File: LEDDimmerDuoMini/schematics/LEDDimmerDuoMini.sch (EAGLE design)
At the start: 17 parts, among them IC1 7805T, T1 2N3904, T2 2N3904

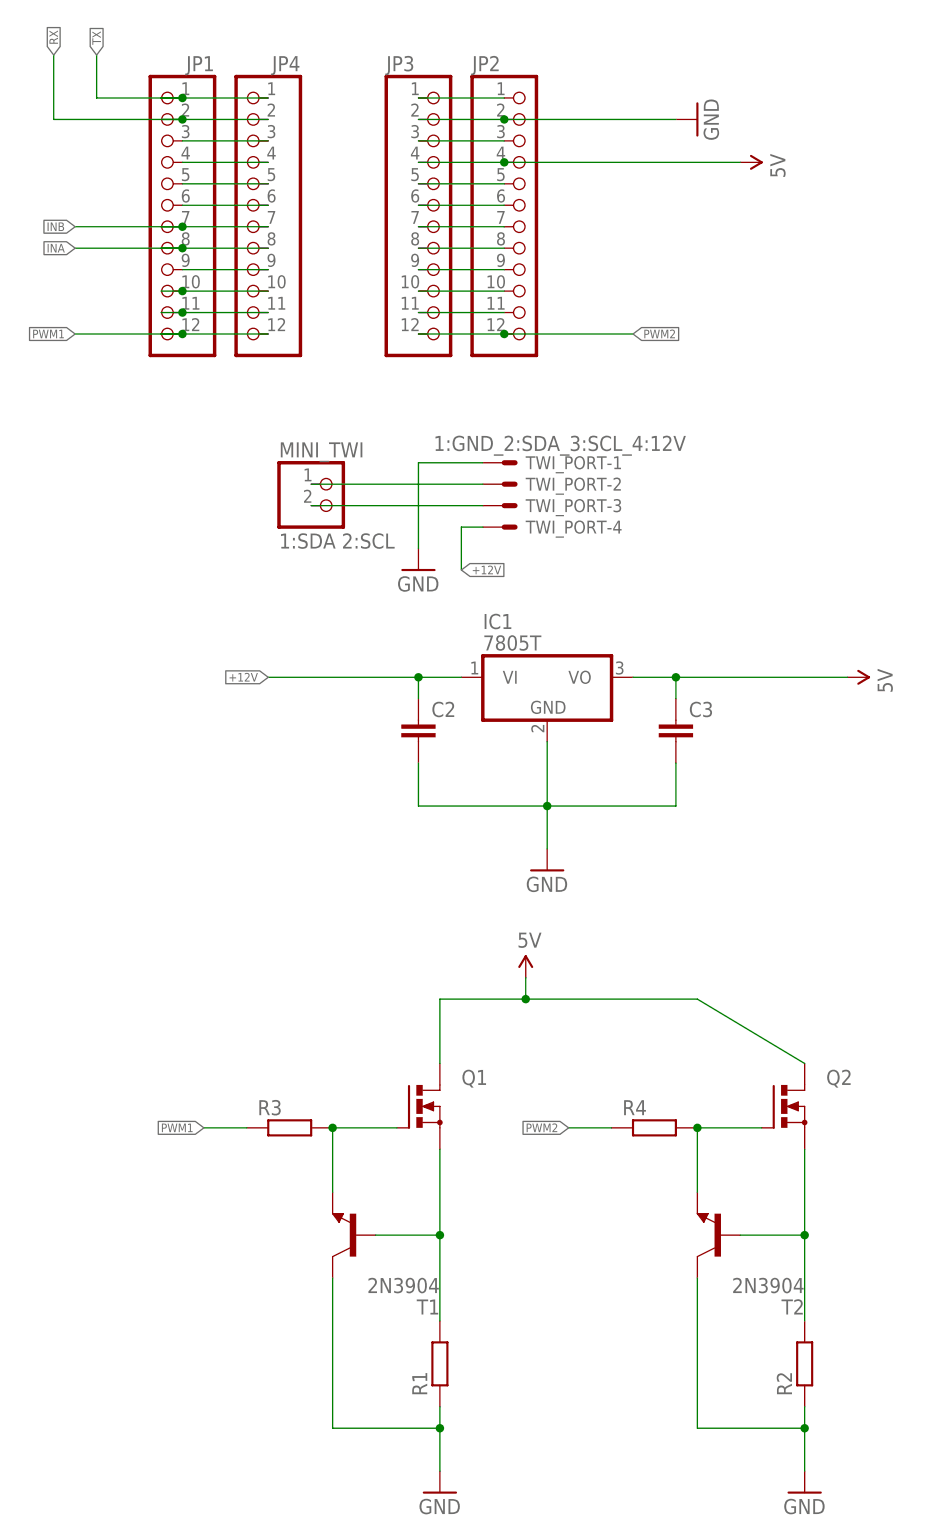
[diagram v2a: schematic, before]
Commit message: Fixed faulty scematic for LEDDimmerDuoMini
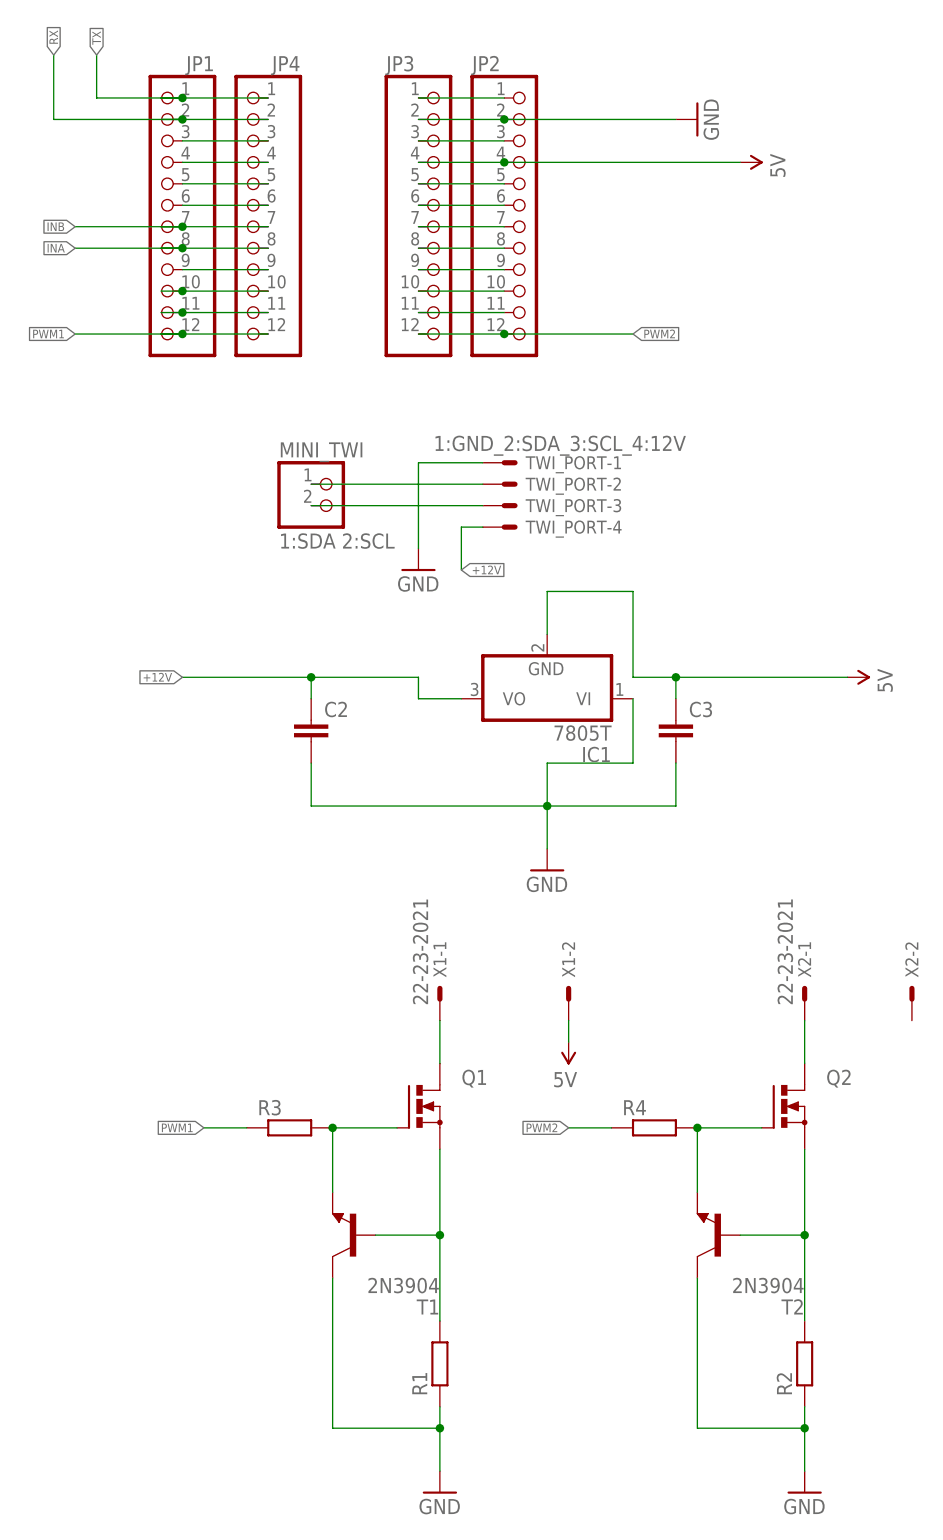
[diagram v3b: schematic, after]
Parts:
- added X1, X2: 22-23-2021, con-molex:22-23-2021
- IC1: device adafruit:7805T -> linear:7805T
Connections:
- new net N$26: Q1.D, X1-1.S
- new net N$27: Q2.D, X2-1.S
- net +12V: now also IC1.VO; no longer IC1.VI
- net 5V: now also IC1.GND, X1-2.S; no longer IC1.VO, Q1.D, Q2.D
- net GND: now also IC1.VI; no longer IC1.GND
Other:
- moved on the sheet: C2, IC1
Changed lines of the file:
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@@
 </classes>
 <parts>
-<part name="IC1" library="adafruit" deviceset="78*" device="T" technology="05" value="7805T"/>
 <part name="C2" library="SparkFun-Capacitors" deviceset="CAP" device="0603-CAP"/>
 <part name="C3" library="SparkFun-Capacitors" deviceset="CAP" device="0603-CAP"/>
@@
 <part name="JP3" library="pinhead" deviceset="PINHD-1X12" device=""/>
 <part name="JP4" library="pinhead" deviceset="PINHD-1X12" device=""/>
+<part name="X1" library="con-molex" deviceset="22-23-2021" device=""/>
+<part name="X2" library="con-molex" deviceset="22-23-2021" device=""/>
+<part name="IC1" library="linear" deviceset="78*" device="T" technology="05"/>
 </parts>
 <sheets>
@@
 </plain>
 <instances>
-<instance part="IC1" gate="A1" x="104.14" y="58.42"/>
-<instance part="C2" gate="G$1" x="88.9" y="50.8"/>
+<instance part="C2" gate="G$1" x="76.2" y="50.8"/>
 <instance part="C3" gate="G$1" x="119.38" y="50.8"/>
 <instance part="GND1" gate="1" x="104.14" y="35.56"/>
@@
 <instance part="T1" gate="G1" x="81.28" y="-7.62" rot="R180"/>
 <instance part="R1" gate="G$1" x="91.44" y="-22.86" rot="R90"/>
-<instance part="SUPPLY1" gate="G$1" x="101.6" y="22.86"/>
+<instance part="SUPPLY1" gate="G$1" x="106.68" y="15.24" rot="R180"/>
 <instance part="GND3" gate="1" x="91.44" y="-38.1"/>
 <instance part="Q2" gate="G$1" x="132.08" y="7.62"/>
@@
 <instance part="JP3" gate="G$1" x="91.44" y="114.3"/>
 <instance part="JP4" gate="G$1" x="68.58" y="114.3" rot="MR0"/>
+<instance part="X1" gate="-1" x="91.44" y="20.32" rot="R90"/>
+<instance part="X1" gate="-2" x="106.68" y="20.32" rot="R90"/>
+<instance part="X2" gate="-1" x="134.62" y="20.32" rot="R90"/>
+<instance part="X2" gate="-2" x="147.32" y="20.32" rot="R90"/>
+<instance part="IC1" gate="A1" x="104.14" y="55.88" rot="R180"/>
 </instances>
 <busses>
@@
 <segment>
 <pinref part="GND1" gate="1" pin="GND"/>
-<pinref part="IC1" gate="A1" pin="GND"/>
 <wire x1="104.14" y1="38.1" x2="104.14" y2="43.18" width="0.1524" layer="91"/>
-<wire x1="104.14" y1="43.18" x2="104.14" y2="50.8" width="0.1524" layer="91"/>
 <junction x="104.14" y="43.18"/>
 <pinref part="C2" gate="G$1" pin="2"/>
-<wire x1="88.9" y1="43.18" x2="104.14" y2="43.18" width="0.1524" layer="91"/>
-<wire x1="88.9" y1="48.26" x2="88.9" y2="43.18" width="0.1524" layer="91"/>
+<wire x1="76.2" y1="43.18" x2="104.14" y2="43.18" width="0.1524" layer="91"/>
+<wire x1="76.2" y1="48.26" x2="76.2" y2="43.18" width="0.1524" layer="91"/>
 <pinref part="C3" gate="G$1" pin="2"/>
 <wire x1="119.38" y1="48.26" x2="119.38" y2="43.18" width="0.1524" layer="91"/>
 <wire x1="119.38" y1="43.18" x2="104.14" y2="43.18" width="0.1524" layer="91"/>
+<pinref part="IC1" gate="A1" pin="VI"/>
+<wire x1="114.3" y1="55.88" x2="114.3" y2="48.26" width="0.1524" layer="91"/>
+<wire x1="114.3" y1="48.26" x2="104.14" y2="48.26" width="0.1524" layer="91"/>
+<wire x1="104.14" y1="48.26" x2="104.14" y2="43.18" width="0.1524" layer="91"/>
 </segment>
 <segment>
@@
 <net name="+12V" class="0">
 <segment>
-<wire x1="88.9" y1="58.42" x2="71.12" y2="58.42" width="0.1524" layer="91"/>
-<label x="71.12" y="58.42" size="1.016" layer="95" rot="MR0" xref="yes"/>
-<pinref part="IC1" gate="A1" pin="VI"/>
+<wire x1="76.2" y1="58.42" x2="60.96" y2="58.42" width="0.1524" layer="91"/>
+<label x="60.96" y="58.42" size="1.016" layer="95" rot="MR0" xref="yes"/>
 <pinref part="C2" gate="G$1" pin="1"/>
-<wire x1="88.9" y1="58.42" x2="93.98" y2="58.42" width="0.1524" layer="91"/>
-<wire x1="88.9" y1="55.88" x2="88.9" y2="58.42" width="0.1524" layer="91"/>
-<junction x="88.9" y="58.42"/>
+<wire x1="76.2" y1="55.88" x2="76.2" y2="58.42" width="0.1524" layer="91"/>
+<wire x1="76.2" y1="58.42" x2="88.9" y2="58.42" width="0.1524" layer="91"/>
+<junction x="76.2" y="58.42"/>
+<wire x1="88.9" y1="58.42" x2="88.9" y2="55.88" width="0.1524" layer="91"/>
+<pinref part="IC1" gate="A1" pin="VO"/>
+<wire x1="88.9" y1="55.88" x2="93.98" y2="55.88" width="0.1524" layer="91"/>
 </segment>
 <segment>
@@
 </segment>
 <segment>
-<pinref part="IC1" gate="A1" pin="VO"/>
 <pinref part="SUPPLY4" gate="G$1" pin="5V"/>
-<wire x1="114.3" y1="58.42" x2="119.38" y2="58.42" width="0.1524" layer="91"/>
 <pinref part="C3" gate="G$1" pin="1"/>
 <wire x1="119.38" y1="58.42" x2="139.7" y2="58.42" width="0.1524" layer="91"/>
 <wire x1="119.38" y1="55.88" x2="119.38" y2="58.42" width="0.1524" layer="91"/>
 <junction x="119.38" y="58.42"/>
-</segment>
-<segment>
-<wire x1="91.44" y1="20.32" x2="101.6" y2="20.32" width="0.1524" layer="91"/>
-<wire x1="101.6" y1="20.32" x2="121.92" y2="20.32" width="0.1524" layer="91"/>
-<wire x1="101.6" y1="20.32" x2="101.6" y2="22.86" width="0.1524" layer="91"/>
-<junction x="101.6" y="20.32"/>
+<wire x1="119.38" y1="58.42" x2="114.3" y2="58.42" width="0.1524" layer="91"/>
+<wire x1="114.3" y1="58.42" x2="114.3" y2="68.58" width="0.1524" layer="91"/>
+<wire x1="114.3" y1="68.58" x2="104.14" y2="68.58" width="0.1524" layer="91"/>
+<pinref part="IC1" gate="A1" pin="GND"/>
+<wire x1="104.14" y1="68.58" x2="104.14" y2="63.5" width="0.1524" layer="91"/>
+</segment>
+<segment>
 <pinref part="SUPPLY1" gate="G$1" pin="5V"/>
-<pinref part="Q1" gate="G$1" pin="D"/>
-<wire x1="91.44" y1="20.32" x2="91.44" y2="12.7" width="0.1524" layer="91"/>
-<pinref part="Q2" gate="G$1" pin="D"/>
-<wire x1="134.62" y1="12.7" x2="121.92" y2="20.32" width="0.1524" layer="91"/>
+<wire x1="106.68" y1="15.24" x2="106.68" y2="17.78" width="0.1524" layer="91"/>
+<pinref part="X1" gate="-2" pin="S"/>
 </segment>
 </net>
@@
 </segment>
 </net>
+<net name="N$26" class="0">
+<segment>
+<pinref part="Q1" gate="G$1" pin="D"/>
+<wire x1="91.44" y1="17.78" x2="91.44" y2="12.7" width="0.1524" layer="91"/>
+<pinref part="X1" gate="-1" pin="S"/>
+</segment>
+</net>
+<net name="N$27" class="0">
+<segment>
+<pinref part="Q2" gate="G$1" pin="D"/>
+<wire x1="134.62" y1="17.78" x2="134.62" y2="12.7" width="0.1524" layer="91"/>
+<pinref part="X2" gate="-1" pin="S"/>
+</segment>
+</net>

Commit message: HOK post laptop update
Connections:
- net GND: now also X2-2.S
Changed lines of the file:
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@@
 <wire x1="121.92" y1="-30.48" x2="134.62" y2="-30.48" width="0.1524" layer="91"/>
 <junction x="134.62" y="-30.48"/>
+<wire x1="134.62" y1="-30.48" x2="147.32" y2="-30.48" width="0.1524" layer="91"/>
+<pinref part="X2" gate="-2" pin="S"/>
+<wire x1="147.32" y1="-30.48" x2="147.32" y2="17.78" width="0.1524" layer="91"/>
 </segment>
 </net>
